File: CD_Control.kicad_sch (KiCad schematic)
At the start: 70 parts, among them Q10 ASR65R046EFD, Q11 ASR65R046EFD, Q12 ASR65R046EFD, Q13 ASR65R046EFD, Q14 ASR65R046EFD, Q15 ASR65R046EFD, Q16 ASR65R046EFD, Q17 AO3400A, Q18 AO3400A, Q19 ASR65R046EFD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

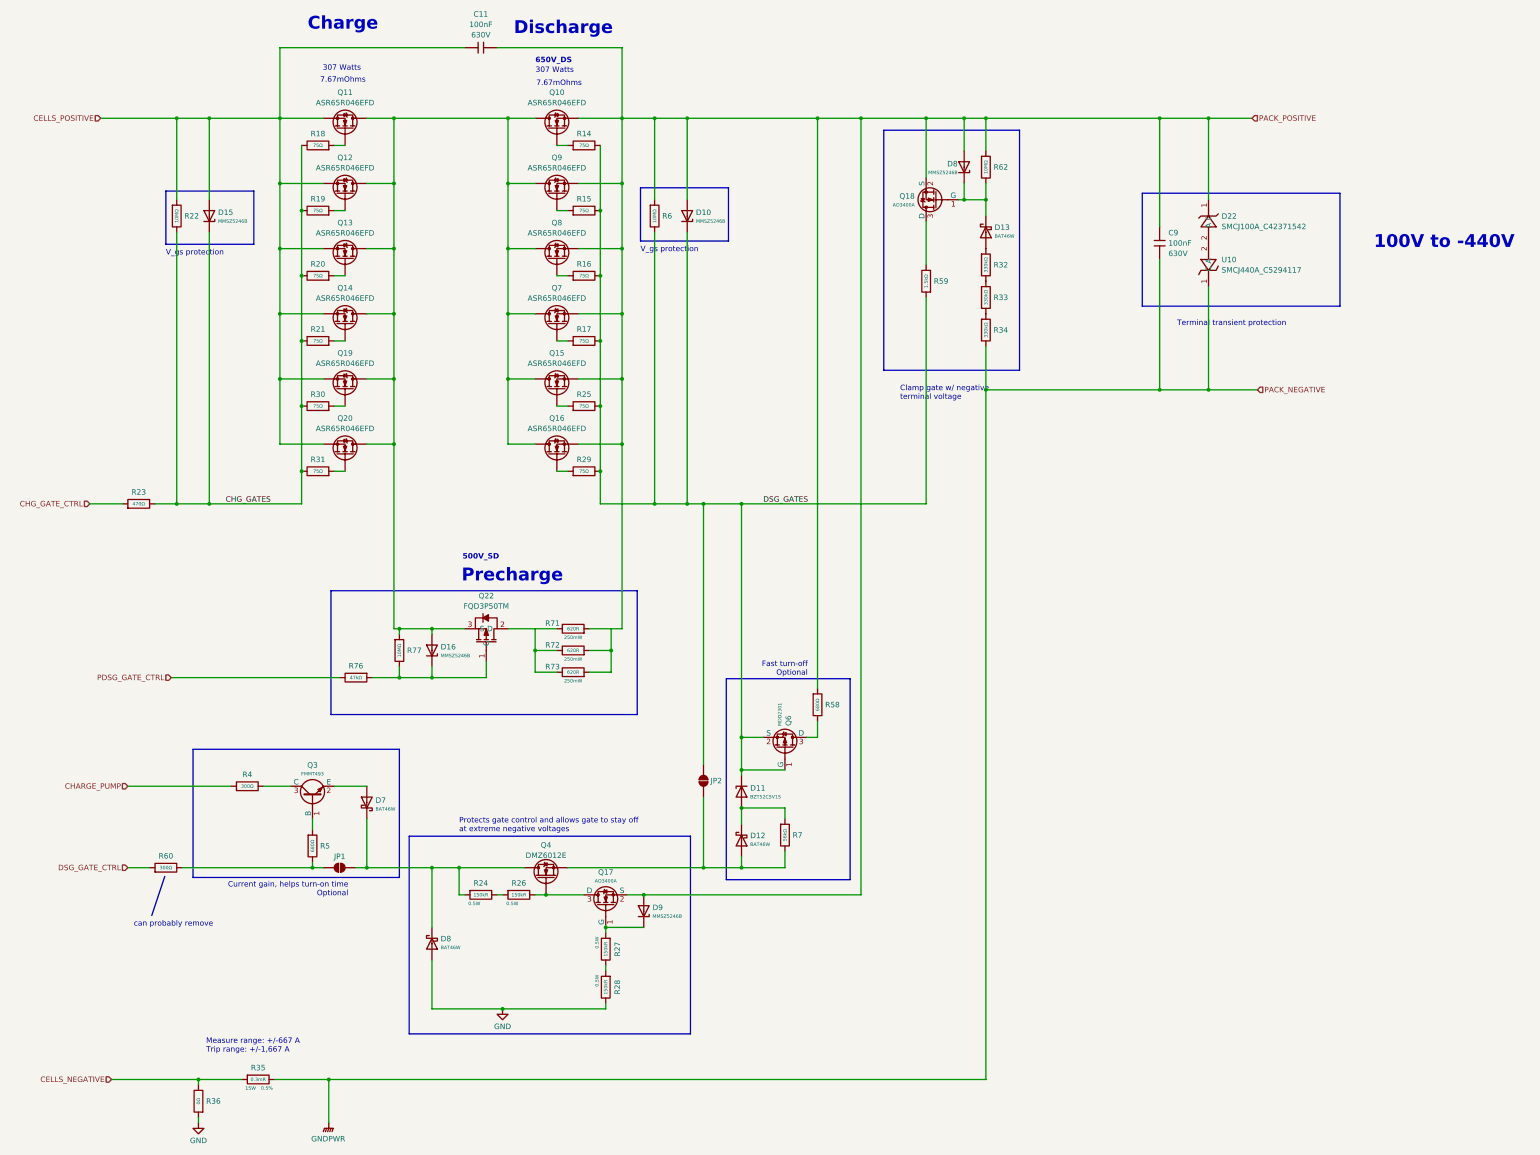
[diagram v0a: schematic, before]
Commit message: Revert "added precharge circuit, filled in placeholder parts"
This reverts commit caa5444a50fe9d2ccb2e95970e40619801e9f697.
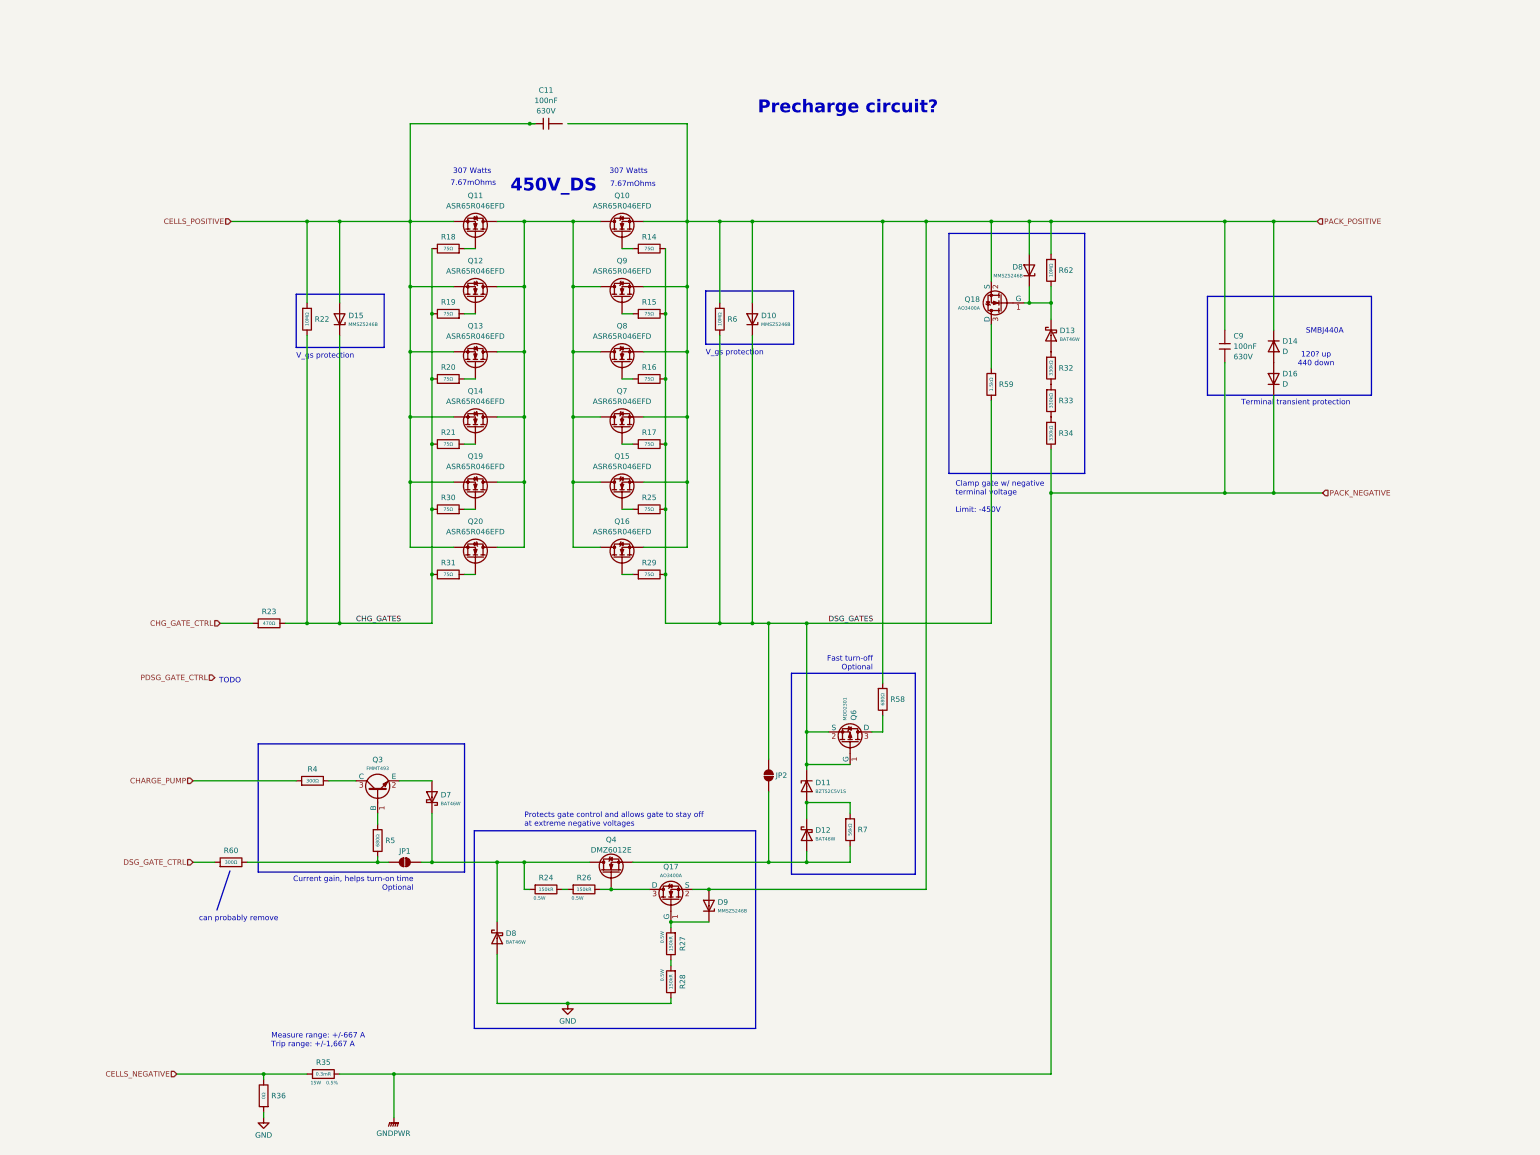
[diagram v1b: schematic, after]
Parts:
- removed D16: MMSZ5246B, PCM_JLCPCB:D_SOD-123, symbol PCM_JLCPCB-Diodes:Zener,MMSZ5246B
- removed D22: SMCJ100A_C42371542, JLCImport:SMCJ100A_C42371542, symbol JLCImport:SMCJ100A_C42371542
- removed Q22: FQD3P50TM, PCM_JLCPCB:TO-252-2_L6.5-W6.1-P4.58-LS10.0-TL, symbol JLCImport:FQD3P50TM
- removed R71, R72, R73: 620R, PCM_JLCPCB:R_1206, symbol ct_lib:1206W4F6200T5E
- removed R76: 47kΩ, PCM_JLCPCB:R_0402, symbol PCM_JLCPCB-Resistors:0402,47kΩ
- removed R77: 10MΩ, PCM_JLCPCB:R_0402, symbol PCM_JLCPCB-Resistors:0402,10MΩ
- removed U10: SMCJ440A_C5294117, PCM_JLCPCB:SOIC-8_L4.9-W3.9-P1.27-LS6.0-BL, symbol JLCImport:SMCJ440A_C5294117
- added D14, D16: D, symbol Device:D
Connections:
- net GNDPWR: now also D16.1 (K)
- net PACK_POSITIVE: now also D14.1 (K); no longer C11.2
- new net: D14.2 (A), D16.2 (A)
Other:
- note added: "120? up 440 down"
- note added: "450V_DS"
- note added: "Clamp gate w/ negative terminal voltage Limit: -450V"
- note added: "Precharge circuit?"
- note added: "SMBJ440A"
- note added: "TODO"
- note removed: "100V to -440V"
- note removed: "500V_SD"
- note removed: "650V_DS"
- note removed: "Charge"
- note removed: "Clamp gate w/ negative terminal voltage"
- note removed: "Discharge"
- note removed: "Precharge"
- moved on the sheet: C11, C9, D10, D11, D12, D13, D15, D7, D8, D9, JP1, JP2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
